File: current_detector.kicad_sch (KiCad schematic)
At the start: 7 parts, among them J1201 tracks, J1202 ter, J1203 ter, U1201 EL814

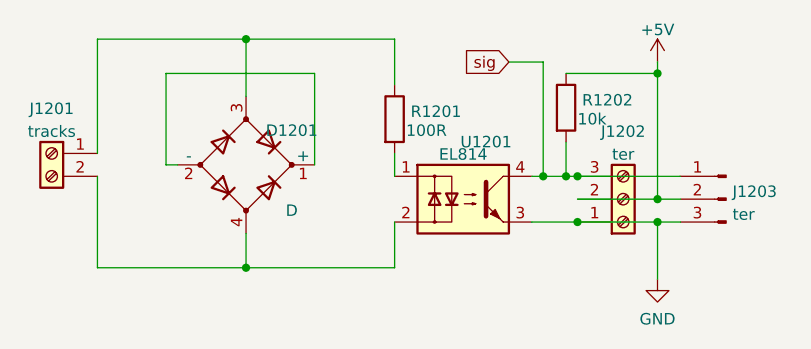
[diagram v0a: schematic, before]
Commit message: added hierarchial labels to some schematics
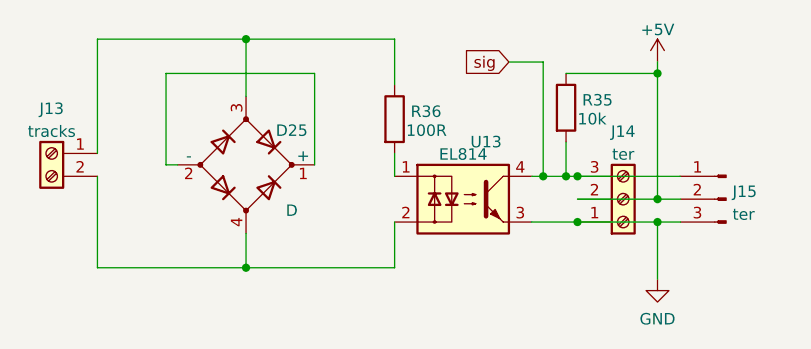
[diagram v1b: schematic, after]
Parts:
- renumbered D1201 to D25, J1201 to J13, J1202 to J14, J1203 to J15, R1202 to R35, R1201 to R36, U1201 to U13

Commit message: moved some schematic scheets to their own folders and routed a board with it. This allow for re-use of PCB parts.
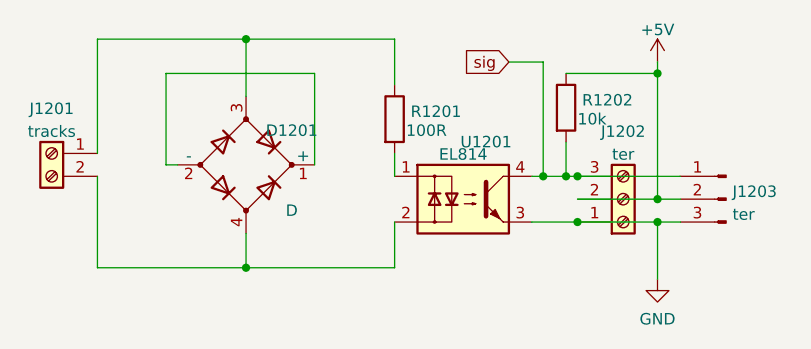
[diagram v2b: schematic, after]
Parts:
- renumbered D25 to D1201, J13 to J1201, J14 to J1202, J15 to J1203, R36 to R1201, R35 to R1202, U13 to U1201
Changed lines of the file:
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@@
   (symbol (lib_id "Device:R") (at 139.7 92.71 0) (unit 1)
     (in_bom yes) (on_board yes) (dnp no)
-    (property "Reference" "R36" (at 141.478 91.8753 0)
+    (property "Reference" "R1201" (at 141.478 91.8753 0)
       (effects (font (size 1.27 1.27)) (justify left))
     )
@@
       (project "general_schematics"
         (path "/e777d9ec-d073-4229-a9e6-2cf85636e407/f6483e49-7b85-4a34-9d17-dfb7f9079bae"
-          (reference "R36") (unit 1)
+          (reference "R1201") (unit 1)
         )
       )
@@
   (symbol (lib_id "Device:D_Bridge_+-AA") (at 123.19 97.79 0) (unit 1)
     (in_bom yes) (on_board yes) (dnp no)
-    (property "Reference" "D25" (at 128.27 93.98 0)
+    (property "Reference" "D1201" (at 128.27 93.98 0)
       (effects (font (size 1.27 1.27)))
     )
@@
       (project "general_schematics"
         (path "/e777d9ec-d073-4229-a9e6-2cf85636e407/f6483e49-7b85-4a34-9d17-dfb7f9079bae"
-          (reference "D25") (unit 1)
+          (reference "D1201") (unit 1)
         )
       )
@@
   (symbol (lib_id "Device:R") (at 158.75 91.44 0) (unit 1)
     (in_bom yes) (on_board yes) (dnp no)
-    (property "Reference" "R35" (at 160.528 90.6053 0)
+    (property "Reference" "R1202" (at 160.528 90.6053 0)
       (effects (font (size 1.27 1.27)) (justify left))
     )
@@
       (project "general_schematics"
         (path "/e777d9ec-d073-4229-a9e6-2cf85636e407/f6483e49-7b85-4a34-9d17-dfb7f9079bae"
-          (reference "R35") (unit 1)
+          (reference "R1202") (unit 1)
         )
       )
@@
   (symbol (lib_id "Connector:Conn_01x03_Male") (at 176.53 101.6 0) (mirror y) (unit 1)
     (in_bom yes) (on_board yes) (dnp no) (fields_autoplaced)
-    (property "Reference" "J15" (at 177.2412 100.7653 0)
+    (property "Reference" "J1203" (at 177.2412 100.7653 0)
       (effects (font (size 1.27 1.27)) (justify right))
     )
@@
       (project "general_schematics"
         (path "/e777d9ec-d073-4229-a9e6-2cf85636e407/f6483e49-7b85-4a34-9d17-dfb7f9079bae"
-          (reference "J15") (unit 1)
+          (reference "J1203") (unit 1)
         )
       )
@@
   (symbol (lib_id "Connector:Screw_Terminal_01x02") (at 101.6 96.52 0) (mirror y) (unit 1)
     (in_bom yes) (on_board yes) (dnp no) (fields_autoplaced)
-    (property "Reference" "J13" (at 101.6 91.5502 0)
+    (property "Reference" "J1201" (at 101.6 91.5502 0)
       (effects (font (size 1.27 1.27)))
     )
@@
       (project "general_schematics"
         (path "/e777d9ec-d073-4229-a9e6-2cf85636e407/f6483e49-7b85-4a34-9d17-dfb7f9079bae"
-          (reference "J13") (unit 1)
+          (reference "J1201") (unit 1)
         )
       )
@@
   (symbol (lib_id "Connector:Screw_Terminal_01x03") (at 165.1 101.6 0) (mirror x) (unit 1)
     (in_bom yes) (on_board yes) (dnp no) (fields_autoplaced)
-    (property "Reference" "J14" (at 165.1 94.0902 0)
+    (property "Reference" "J1202" (at 165.1 94.0902 0)
       (effects (font (size 1.27 1.27)))
     )
@@
       (project "general_schematics"
         (path "/e777d9ec-d073-4229-a9e6-2cf85636e407/f6483e49-7b85-4a34-9d17-dfb7f9079bae"
-          (reference "J14") (unit 1)
+          (reference "J1202") (unit 1)
         )
       )
@@
   (symbol (lib_id "power:+5V") (at 168.91 86.36 0) (unit 1)
     (in_bom yes) (on_board yes) (dnp no) (fields_autoplaced)
-    (property "Reference" "#PWR049" (at 168.91 90.17 0)
+    (property "Reference" "#PWR0134" (at 168.91 90.17 0)
       (effects (font (size 1.27 1.27)) hide)
     )
@@
       (project "general_schematics"
         (path "/e777d9ec-d073-4229-a9e6-2cf85636e407/f6483e49-7b85-4a34-9d17-dfb7f9079bae"
-          (reference "#PWR049") (unit 1)
+          (reference "#PWR0134") (unit 1)
         )
       )
@@
   (symbol (lib_id "power:GND") (at 168.91 110.49 0) (unit 1)
     (in_bom yes) (on_board yes) (dnp no) (fields_autoplaced)
-    (property "Reference" "#PWR050" (at 168.91 116.84 0)
+    (property "Reference" "#PWR0133" (at 168.91 116.84 0)
       (effects (font (size 1.27 1.27)) hide)
     )
@@
       (project "general_schematics"
         (path "/e777d9ec-d073-4229-a9e6-2cf85636e407/f6483e49-7b85-4a34-9d17-dfb7f9079bae"
-          (reference "#PWR050") (unit 1)
+          (reference "#PWR0133") (unit 1)
         )
       )
@@
   (symbol (lib_id "Isolator:EL814") (at 147.32 101.6 0) (unit 1)
     (in_bom yes) (on_board yes) (dnp no)
-    (property "Reference" "U13" (at 149.86 95.25 0)
+    (property "Reference" "U1201" (at 149.86 95.25 0)
       (effects (font (size 1.27 1.27)))
     )
@@
       (project "general_schematics"
         (path "/e777d9ec-d073-4229-a9e6-2cf85636e407/f6483e49-7b85-4a34-9d17-dfb7f9079bae"
-          (reference "U13") (unit 1)
-        )
-      )
+          (reference "U1201") (unit 1)
+        )
+      )
